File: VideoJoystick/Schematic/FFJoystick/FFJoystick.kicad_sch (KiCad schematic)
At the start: 5 parts, among them J1 Raspberry_Pi_2_3, U1 LTC1661CN8-PBF, U2 RCD-24

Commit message: Put connectors into the schematic.
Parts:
- added J2: Joystick Out, symbol Connector_Generic:Conn_01x03
- added J3: ~, symbol Connector:Conn_01x04_Pin
- added J4: ~, symbol Connector:Conn_01x04_Socket
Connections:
- net GND: now also J2.2 (Pin_2)
- net at R1.1, U2.3 (PWM/ON/OFF): now also J3.4 (Pin_4); no longer J1.32 (PWM0/GPIO12)
- net at J1.19 (MOSI0/GPIO10): now also J4.3 (Pin_3); no longer U1.3 (DIN)
- net at J1.23 (SCLK0/GPIO11): now also J4.2 (Pin_2); no longer U1.2 (SCK)
- net at J1.24 (~{CE0}/GPIO8): now also J4.1 (Pin_1); no longer U1.1 (*CS/LD)
- net at U1.5 (VOUTB): now also J2.3 (Pin_3)
- net at U1.8 (VOUTA): now also J2.1 (Pin_1)
- new net: J1.32 (PWM0/GPIO12), J4.4 (Pin_4)
- new net: J3.1 (Pin_1), U1.1 (*CS/LD)
- new net: J3.2 (Pin_2), U1.2 (SCK)
- new net: J3.3 (Pin_3), U1.3 (DIN)
- no-connect marks 0 -> 1
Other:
- moved on the sheet: D1, J1, R1, U1, U2

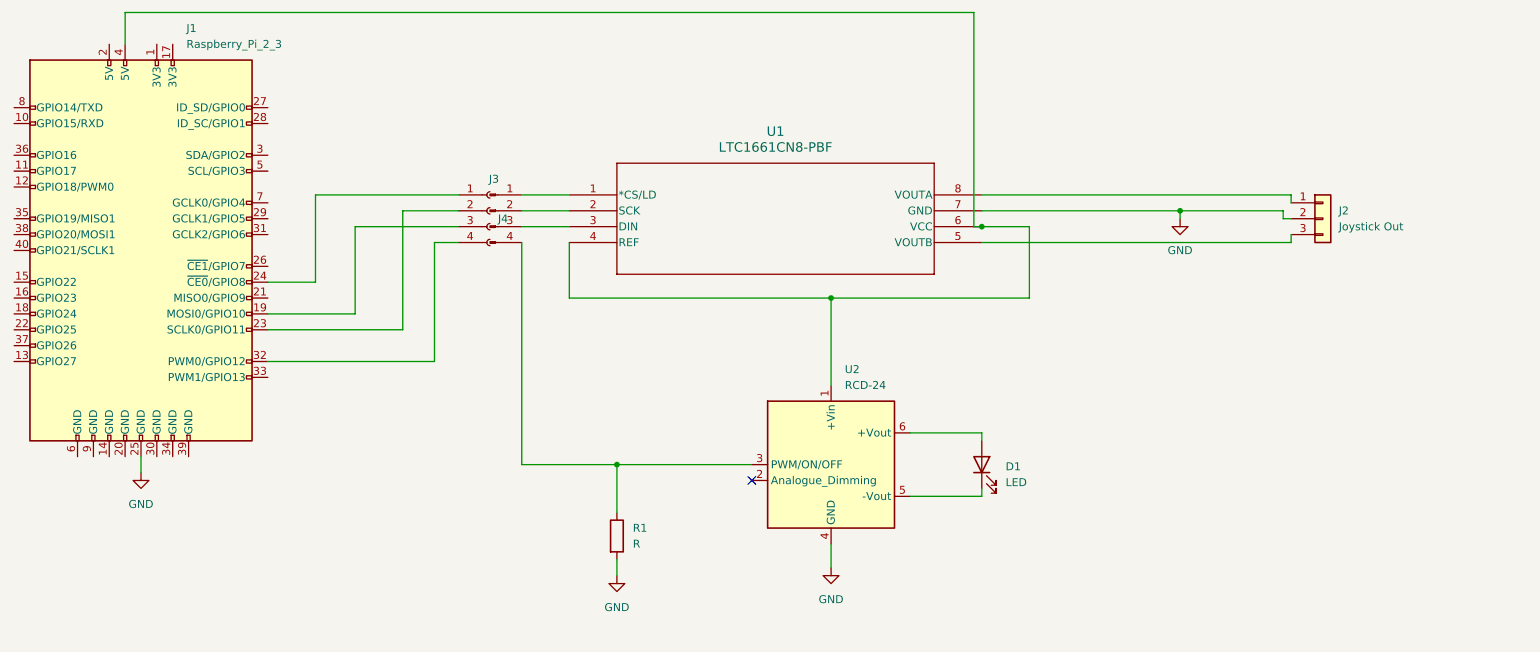
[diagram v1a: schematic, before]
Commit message: Made better sense of the connectors on the schematic
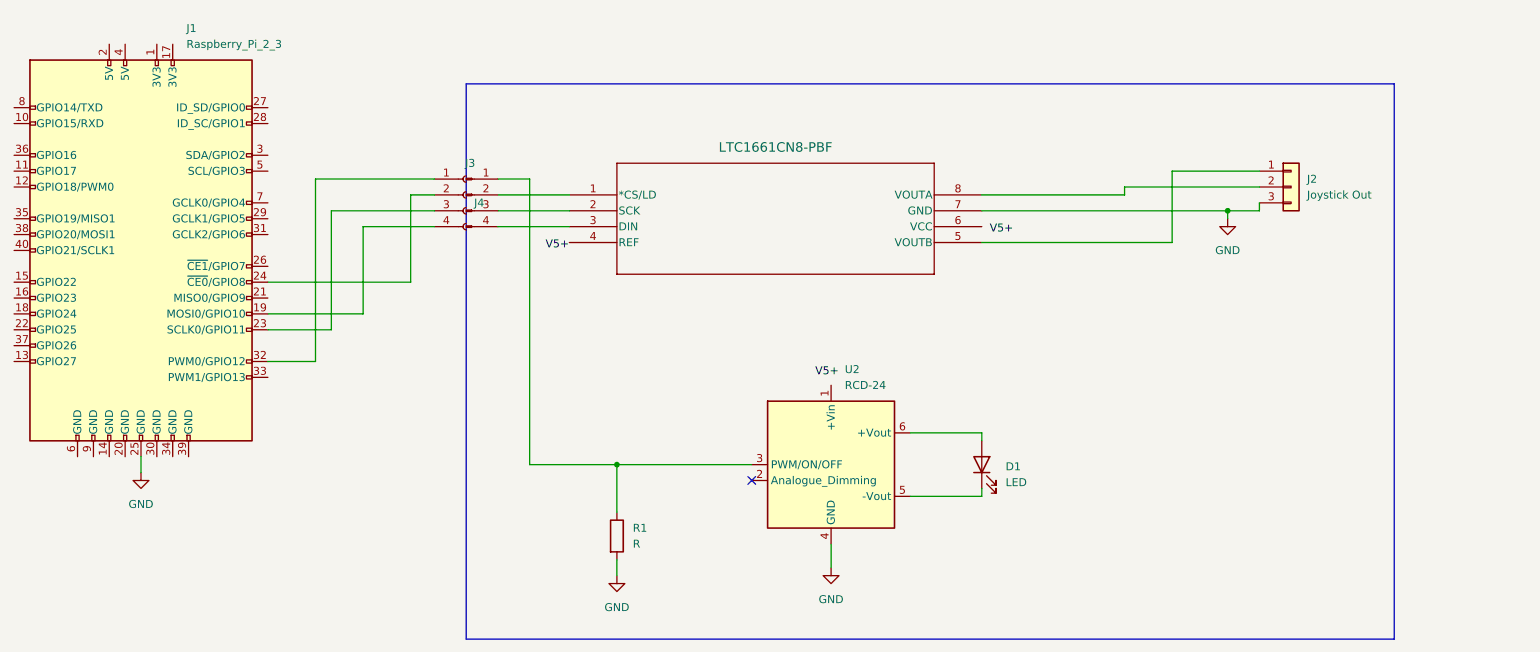
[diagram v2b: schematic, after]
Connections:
- net GND: now also J2.3 (Pin_3); no longer J2.2 (Pin_2)
- net at J4.1 (Pin_1): now also J1.32 (PWM0/GPIO12); no longer J1.24 (~{CE0}/GPIO8)
- net at J4.2 (Pin_2): now also J1.24 (~{CE0}/GPIO8); no longer J1.23 (SCLK0/GPIO11)
- net at J4.3 (Pin_3): now also J1.23 (SCLK0/GPIO11); no longer J1.19 (MOSI0/GPIO10)
- net at J4.4 (Pin_4): now also J1.19 (MOSI0/GPIO10); no longer J1.32 (PWM0/GPIO12)
- net at R1.1, U2.3 (PWM/ON/OFF): now also J3.1 (Pin_1); no longer J3.4 (Pin_4)
- net at J2.1 (Pin_1): now also U1.5 (VOUTB); no longer U1.8 (VOUTA)
- net at U1.1 (*CS/LD): now also J3.2 (Pin_2); no longer J3.1 (Pin_1)
- net at U1.2 (SCK): now also J3.3 (Pin_3); no longer J3.2 (Pin_2)
- net at U1.3 (DIN): now also J3.4 (Pin_4); no longer J3.3 (Pin_3)
- new net: J2.2 (Pin_2), U1.8 (VOUTA)
- now unconnected: J1.4 (5V), U1.4 (REF), U1.6 (VCC), U2.1 (+Vin)
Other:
- moved on the sheet: J2, J3, J4

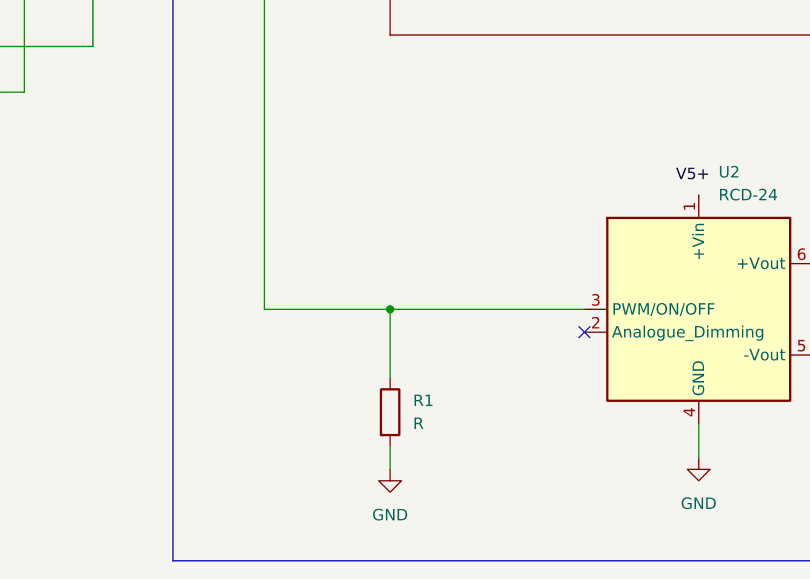
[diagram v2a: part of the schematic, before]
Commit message: Changed the pulldown to a pullup for the LED PWM
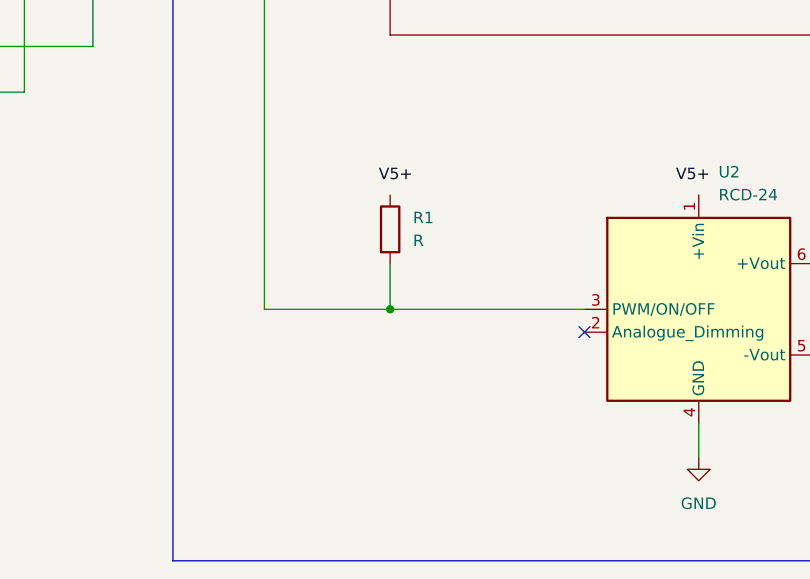
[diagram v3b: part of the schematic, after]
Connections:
- net GND: no longer R1.2
- net at J3.1 (Pin_1), U2.3 (PWM/ON/OFF): now also R1.2; no longer R1.1
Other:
- moved on the sheet: R1
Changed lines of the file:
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@@
-    (stroke (width 0) (type default))
-  )
-  (wire (pts (xy 127 91.44) (xy 127 99.06))
     (stroke (width 0) (type default))
   )
@@
     (stroke (width 0) (type default))
   )
+  (wire (pts (xy 127 86.36) (xy 127 91.44))
+    (stroke (width 0) (type default))
+  )
   (wire (pts (xy 93.98 62.23) (xy 71.12 62.23))
     (stroke (width 0) (type default))
@@
     (stroke (width 0) (type default))
   )
-  (wire (pts (xy 127 106.68) (xy 127 109.22))
-    (stroke (width 0) (type default))
-  )
   (wire (pts (xy 78.74 74.93) (xy 71.12 74.93))
     (stroke (width 0) (type default))
@@
     (stroke (width 0) (type default))
     (fill (type none))
+  )
+  (label "V5+" (at 125.73 77.47 0) (fields_autoplaced)
+    (effects (font (size 1.27 1.27)) (justify left bottom))
   )
   (label "V5+" (at 186.69 54.61 0) (fields_autoplaced)
@@
     )
   )
-  (symbol (lib_id "Device:R") (at 127 102.87 0) (unit 1)
-    (in_bom yes) (on_board yes) (dnp no) (fields_autoplaced)
-    (property "Reference" "R1" (at 129.54 101.6 0)
-      (effects (font (size 1.27 1.27)) (justify left))
-    )
-    (property "Value" "R" (at 129.54 104.14 0)
-      (effects (font (size 1.27 1.27)) (justify left))
-    )
-    (property "Footprint" "" (at 125.222 102.87 90)
-      (effects (font (size 1.27 1.27)) hide)
-    )
-    (property "Datasheet" "~" (at 127 102.87 0)
+  (symbol (lib_id "Device:R") (at 127 82.55 0) (unit 1)
+    (in_bom yes) (on_board yes) (dnp no) (fields_autoplaced)
+    (property "Reference" "R1" (at 129.54 81.28 0)
+      (effects (font (size 1.27 1.27)) (justify left))
+    )
+    (property "Value" "R" (at 129.54 83.82 0)
+      (effects (font (size 1.27 1.27)) (justify left))
+    )
+    (property "Footprint" "" (at 125.222 82.55 90)
+      (effects (font (size 1.27 1.27)) hide)
+    )
+    (property "Datasheet" "~" (at 127 82.55 0)
       (effects (font (size 1.27 1.27)) hide)
     )
@@
         )
       )
-    )
-  )
-  (symbol (lib_id "power:GND") (at 127 109.22 0) (unit 1)
-    (in_bom yes) (on_board yes) (dnp no) (fields_autoplaced)
-    (property "Reference" "#PWR02" (at 127 115.57 0)
-      (effects (font (size 1.27 1.27)) hide)
-    )
-    (property "Value" "GND" (at 127 114.3 0)
-      (effects (font (size 1.27 1.27)))
-    )
-    (property "Footprint" "" (at 127 109.22 0)
-      (effects (font (size 1.27 1.27)) hide)
-    )
-    (property "Datasheet" "" (at 127 109.22 0)
-      (effects (font (size 1.27 1.27)) hide)
-    )
-    (pin "1")
-    (instances
-      (project "FFJoystick"
-        (path "/52e542a9-49cc-4082-a073-0438ca28e208"
-          (reference "#PWR02") (unit 1)
-        )
-      )
